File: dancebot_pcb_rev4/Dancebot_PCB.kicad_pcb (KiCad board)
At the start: 2 copper layers, 53.3 x 63.5 mm, 52 parts, among them J1 Voltage Regulator, J10 NeoPixel Right Eye, J11 Rocker Switch, J2 IO14 servo 1, J3 IO13 servo 2, J4 IO12 servo 3, J5 IO15 servo 4, J6 IO18 servo 5 (hat), J7 UJ2-MIBH2-4-SMT-TR, J8 Pins, J9 NeoPixel Left Eye, Q1 IRLML6402TRPBF, Q2 S8050, Q3 S8050, SW1 RESET, SW2 BOOT, U1 IRLML2502TRPBF, U2 AMS1117-3.3, U3 ESP32-WROOM-32E__4MB_, U4 CP2102N-A02-GQFN28R

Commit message: schematic ready for review!
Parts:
- removed C1: 4.7u, Capacitor_SMD:C_0805_2012Metric
- removed C2: 0.1u, Capacitor_SMD:C_0805_2012Metric
- removed C5: 10u, Capacitor_SMD:C_0805_2012Metric
- removed C6: 22u, Capacitor_SMD:C_0805_2012Metric
- removed D2: 1N5819, Diode_THT:D_DO-41_SOD81_P10.16mm_Horizontal
- removed H4: ~, MountingHole:MountingHole_3.2mm_M3
- removed J1: Voltage Regulator, Connector_PinHeader_2.54mm:PinHeader_1x05_P2.54mm_Vertical
- removed J10: NeoPixel Right Eye, Connector_PinSocket_2.54mm:PinSocket_1x04_P2.54mm_Vertical
- removed J11: Rocker Switch, Connector_PinHeader_2.54mm:PinHeader_1x02_P2.54mm_Vertical
- removed J5: IO15 servo 4, Connector_PinHeader_2.54mm:PinHeader_1x03_P2.54mm_Vertical
- removed J6: IO18 servo 5 (hat), Connector_PinHeader_2.54mm:PinHeader_1x03_P2.54mm_Vertical
- removed J8: Pins, Connector_PinHeader_2.54mm:PinHeader_1x02_P2.54mm_Vertical
- removed TP4: TestPoint, TestPoint:TestPoint_Pad_2.0x2.0mm
- removed U2: AMS1117-3.3, AMS1117-3.3:SOT229P700X180-4N
- removed U3: ESP32-WROOM-32E__4MB_, ESP32-WROOM-32E__4MB_:XCVR_ESP32-WROOM-32E__4MB_
- removed U4: CP2102N-A02-GQFN28R, CP2102N-A02-GQFN28R:IC_CP2102N-A02-GQFN28R
- added C10: 4.7u, SamacSys_Parts:CAPC2013X140N, F.Cu at (252.8, 106.9)
- added C11: 0.1u, SamacSys_Parts:MAJx16, F.Cu at (238.9, 108.5)
- added C201: 1u, SamacSys_Parts:CAPC2012X135N, F.Cu at (221.0, 103.3)
- added C202: 1u, SamacSys_Parts:CAPC2012X135N, F.Cu at (221.0, 106.0)
- added C203: 0.1u, SamacSys_Parts:MAJx16, F.Cu at (215.5, 109.6)
- added C204: 10u, SamacSys_Parts:CAPC1608X80N, F.Cu at (208.1, 109.5)
- added C205: 0.1u, SamacSys_Parts:MAJx16, F.Cu at (215.5, 113.5)
- added C206: 10u, SamacSys_Parts:CAPC1608X80N, F.Cu at (208.1, 111.8)
- added C207: 10u, SamacSys_Parts:CAPC1608X80N, F.Cu at (208.1, 114.1)
- added D201: SMF5.0A_R1_00001, SamacSys_Parts:SMF50A_R1_00001, F.Cu at (221.8, 116.2)
- added D202: LM66100DCKR, SamacSys_Parts:SOP65P210X110-6N, F.Cu at (204.0, 110.2)
- added D203: LM66100DCKR, SamacSys_Parts:SOP65P210X110-6N, F.Cu at (204.0, 113.9)
- added D3: SMF5.0A_R1_00001, SamacSys_Parts:SMF50A_R1_00001, F.Cu at (239.9, 99.2)
- added D303: SMF5.0A_R1_00001, SamacSys_Parts:SMF50A_R1_00001, F.Cu at (239.9, 104.1)
- added H5: MountingHole_Pad, MountingHole:MountingHole_3.2mm_M3, F.Cu at (240.2, 85.9)
- added IC1: CP2102N-A02-GQFN28R, SamacSys_Parts:QFN50P500X500X80-29N-D, F.Cu at (247.2, 103.0)
- added IC2: ESP32-WROOM-32E-N4, SamacSys_Parts:ESP32WROOM32EN4, F.Cu at (212.7, 72.4)
- added IC201: TPS63000IDRCRQ1, SamacSys_Parts:TPS63000IDRCRQ1, F.Cu at (222.3, 98.7)
- added J12: USB_B_Micro, Connector_USB:USB_Micro-B_Amphenol_10118193-0002LF_Horizontal, F.Cu at (248.7, 96.2)
- added J13: Servo 4, Connector_PinHeader_2.54mm:PinHeader_1x03_P2.54mm_Vertical, F.Cu at (252.3, 114.8)
- added J14: Servo 5, Connector_PinHeader_2.54mm:PinHeader_1x03_P2.54mm_Vertical, F.Cu at (256.9, 114.8)
- added J201: BatteryJ ST Connector, SamacSys_Parts:1769, F.Cu at (207.3, 99.6)
- added L201: 2.2u, SamacSys_Parts:NRS3015T2R2MNGHV, F.Cu at (221.2, 110.7)
- added LED1: APT2012PGW, SamacSys_Parts:APT2012PGW, F.Cu at (258.8, 60.2)
- added R201: 100, SamacSys_Parts:RESC2012X50N, F.Cu at (208.6, 116.8)
- added R202: 1M, SamacSys_Parts:RESC2012X60N, F.Cu at (215.2, 116.9)
- added R203: 200k, SamacSys_Parts:RESC1608X55N, F.Cu at (203.7, 117.0)
- added TP201: USBV, TestPoint:TestPoint_Pad_1.0x1.0mm, F.Cu at (214.4, 103.0)
- added TP202: BATV, TestPoint:TestPoint_Pad_1.0x1.0mm, F.Cu at (214.4, 106.1)
- added TP203: BUCK_VIN, TestPoint:TestPoint_Pad_1.0x1.0mm, F.Cu at (217.5, 96.9)
- added TP204: GND, TestPoint:TestPoint_Pad_1.0x1.0mm, F.Cu at (217.5, 100.0)
- added TP205: 3v3, TestPoint:TestPoint_Pad_1.0x1.0mm, F.Cu at (217.5, 103.0)
- C3, C4, C8: footprint Capacitor_SMD:C_0805_2012Metric -> SamacSys_Parts:MAJx16
- C7: footprint Capacitor_SMD:C_0805_2012Metric -> SamacSys_Parts:CAPC2012X145N
- C9: footprint Capacitor_SMD:C_0805_2012Metric -> SamacSys_Parts:CAPC2012X135N
- D1: value LED -> SMF5.0A_R1_00001; footprint LED_SMD:LED_0805_2012Metric -> SamacSys_Parts:SMF50A_R1_00001
- H1, H2, H3: value ~ -> MountingHole_Pad
- J2: value IO14 servo 1 -> Servo 1
- J3: value IO13 servo 2 -> Servo 2
- J4: value IO12 servo 3 -> NeoPixel Left Eye; footprint Connector_PinHeader_2.54mm:PinHeader_1x03_P2.54mm_Vertical -> Connector_PinSocket_2.54mm:PinSocket_1x04_P2.54mm_Vertical
- J7: value UJ2-MIBH2-4-SMT-TR -> Servo #; footprint UJ2-MIBH-4-SMT-TR:CUIDEVICES_UJ2-MIBH-4-SMT-TR -> Connector_PinHeader_2.54mm:PinHeader_1x03_P2.54mm_Vertical
- Q1: footprint IRLML6402TRPBF:SOT95P237X112-3N -> SamacSys_Parts:SOT95P237X112-3N
- Q2, Q3: footprint Package_TO_SOT_THT:TO-92_Inline -> SamacSys_Parts:SOT95P240X115-3N
- R1, R2, R4, R5, R6, R7: footprint Resistor_SMD:R_0805_2012Metric -> SamacSys_Parts:RESC2012X50N
- R10, R13, R8, R9: footprint Resistor_SMD:R_0805_2012Metric -> SamacSys_Parts:RESC2012X60N
- R11, R12: value 2k -> 1k; footprint Resistor_SMD:R_0805_2012Metric -> SamacSys_Parts:RESC2012X60N
- R3: footprint Resistor_SMD:R_0805_2012Metric -> SamacSys_Parts:ERA6AEB101V
- SW1, SW2: footprint Button_Switch_THT:KSA_Tactile_SPST -> SamacSys_Parts:SW_PUSH_6mm
- TP1: value TestPoint -> BATT_ADC; footprint TestPoint:TestPoint_Pad_2.0x2.0mm -> TestPoint:TestPoint_Pad_1.0x1.0mm
- TP2: value TestPoint -> USBC_ST; footprint TestPoint:TestPoint_Pad_2.0x2.0mm -> TestPoint:TestPoint_Pad_1.0x1.0mm
- TP3: value TestPoint -> BAT_ST; footprint TestPoint:TestPoint_Pad_2.0x2.0mm -> TestPoint:TestPoint_Pad_1.0x1.0mm
- U1: footprint IRLML2502TRPBF:SOT23 -> SamacSys_Parts:SOT95P237X112-3N
- moved TP1 101.8 mm to (257.2, 73.8), turned to 0 degrees
- moved H2 100.4 mm to (240.2, 70.0), turned to 0 degrees
- moved R8 91.6 mm to (253.1, 100.9), turned to 0 degrees
- moved J4 91.5 mm to (248.6, 60.4), turned to 0 degrees
- moved H1 89.8 mm to (240.2, 62.0), turned to 0 degrees
- moved J3 88.8 mm to (243.2, 114.8), turned to 0 degrees
- moved R3 88.3 mm to (254.4, 83.7), turned to 0 degrees
- moved R11 86.4 mm to (257.6, 63.9), turned to 0 degrees
- moved Q1 84.7 mm to (253.2, 74.6), turned to 0 degrees
- moved R7 84.0 mm to (245.9, 108.2), turned to 0 degrees
- moved R2 83.0 mm to (248.5, 76.9), turned to 0 degrees
- moved J2 80.7 mm to (238.6, 114.8), turned to 0 degrees
- moved C3 77.0 mm to (226.3, 77.1), turned to 0 degrees
- moved R1 76.7 mm to (248.5, 73.8)
- moved R4 75.6 mm to (248.5, 79.9), turned to 0 degrees
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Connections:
- net BATT ADC renamed /BATTERY_STAT/BATT_ADC
- net DTR renamed /MCU/UART.DTR
- net EN renamed /MCU/EN
- net IO0 renamed /MCU/IO0
- net RTS renamed /MCU/UART.RTS
- C7 pad 1: 3v3 -> +3V3
- C8 pad 1: 3v3 -> +3V3
- D1 pad 1: Net-(D1-K) -> /MCU/D+
- D1 pad 2: 3v3 -> GND
- J2 pad 1: SM1 -> /MCU/SM1
- J2 pad 2: VBUS -> +3V3
- J3 pad 1: SM2 -> /MCU/SM2
- J3 pad 2: VBUS -> +3V3
- J4 pad 1: SM3 -> GND
- J4 pad 2: VBUS -> /LEDS/NP2_DIN
- J4 pad 3: GND -> /LEDS/NP2_DOUT
- J7 pad 1: VBUS -> /MCU/SM3
- J7 pad 2: D- -> +3V3
- J7 pad 3: D+ -> GND
- J9 pad 1: unconnected-(J9-Pin_1-Pad1) -> GND
- J9 pad 2: GND -> /LEDS/NP1_DIN
- J9 pad 3: VOUT -> /LEDS/NP1_DOUT
- J9 pad 4: NPLeftEye -> +3V3
- R11 pad 1: 3v3 -> Net-(LED1-K)
- R11 pad 2: Net-(U4-~{RST}) -> GND
- R12 pad 1: Net-(D1-K) -> +3V3
- R12 pad 2: GND -> Net-(IC1-RSTB)
- R13 pad 1: 3v3 -> +3V3
- R4 pad 1: BATT EN -> /BATTERY_STAT/BATT_EN
- R7 pad 1: VBUS -> /POWER/USB_VBUS
- TP2 pad 1: NPLeftEye -> /POWER/USBC_ST
- TP3 pad 1: NPRightEye -> /POWER/BAT_ST
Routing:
- net SM5: track 15.5 -> 0.00 mm
- net SM4: track 13.5 -> 0.00 mm
- net SM3: track 11.9 -> 0.00 mm
- net D+: track 11.8 -> 0.00 mm, vias 1 -> 0
- net SM2: track 8.71 -> 0.00 mm
- net D-: track 8.27 -> 0.00 mm
- net SM1: track 7.31 -> 0.00 mm
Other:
- board size 53.3 x 63.5 mm -> 53.9 x 63.5 mm
- board text removed: "ADC"
- board text removed: "BATTPWR"
- board text removed: "L"
- board text removed: "R"
- board text removed: "aL"
- board text removed: "aR"
- board text removed: "hL"
- board text removed: "hR"
- board text removed: "hat"

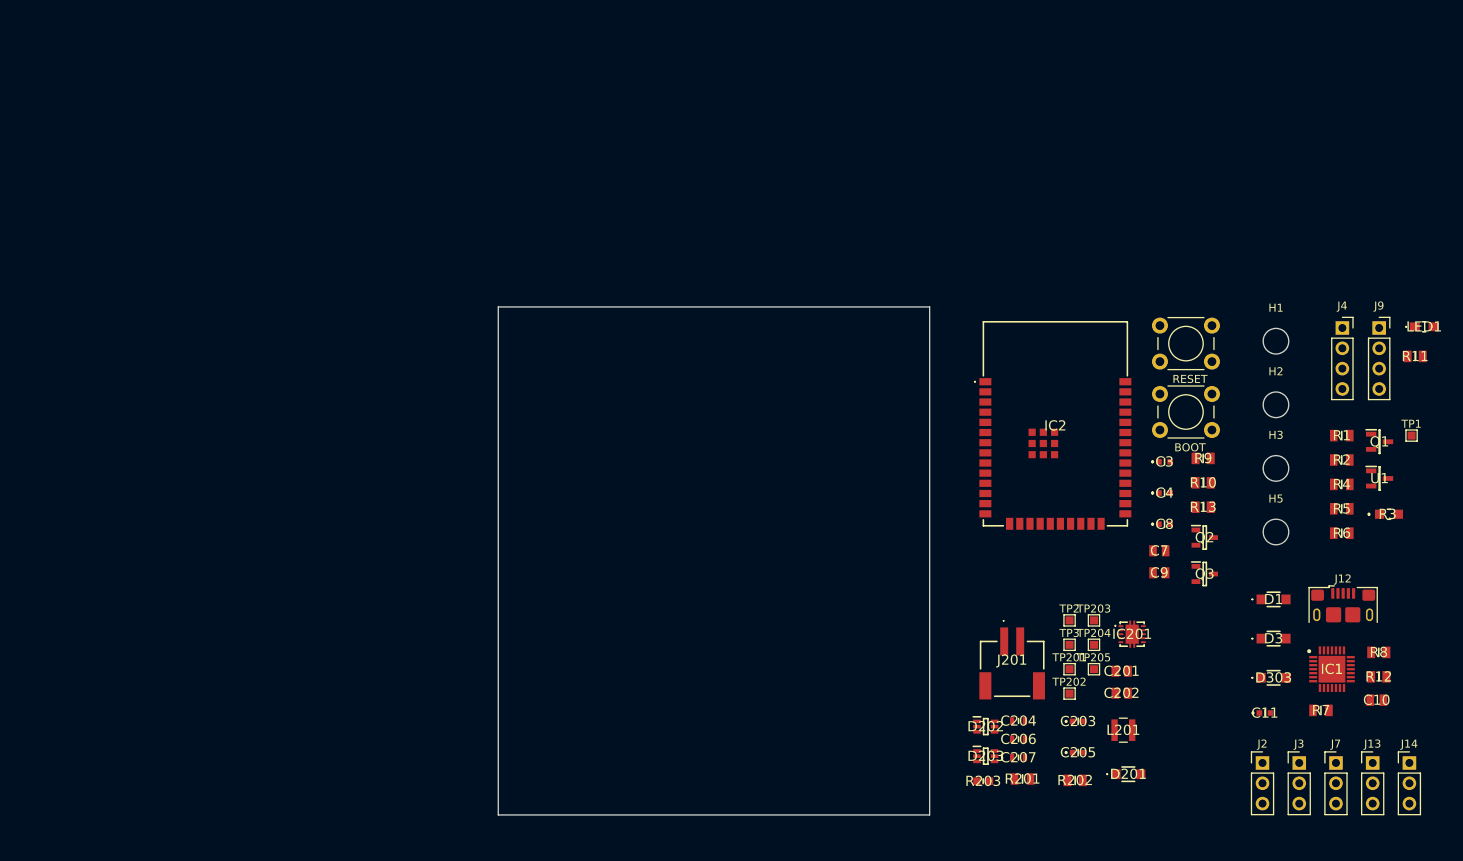
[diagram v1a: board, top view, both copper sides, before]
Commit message: now using ESP32-S3-WROOM-1, changed power delivery system
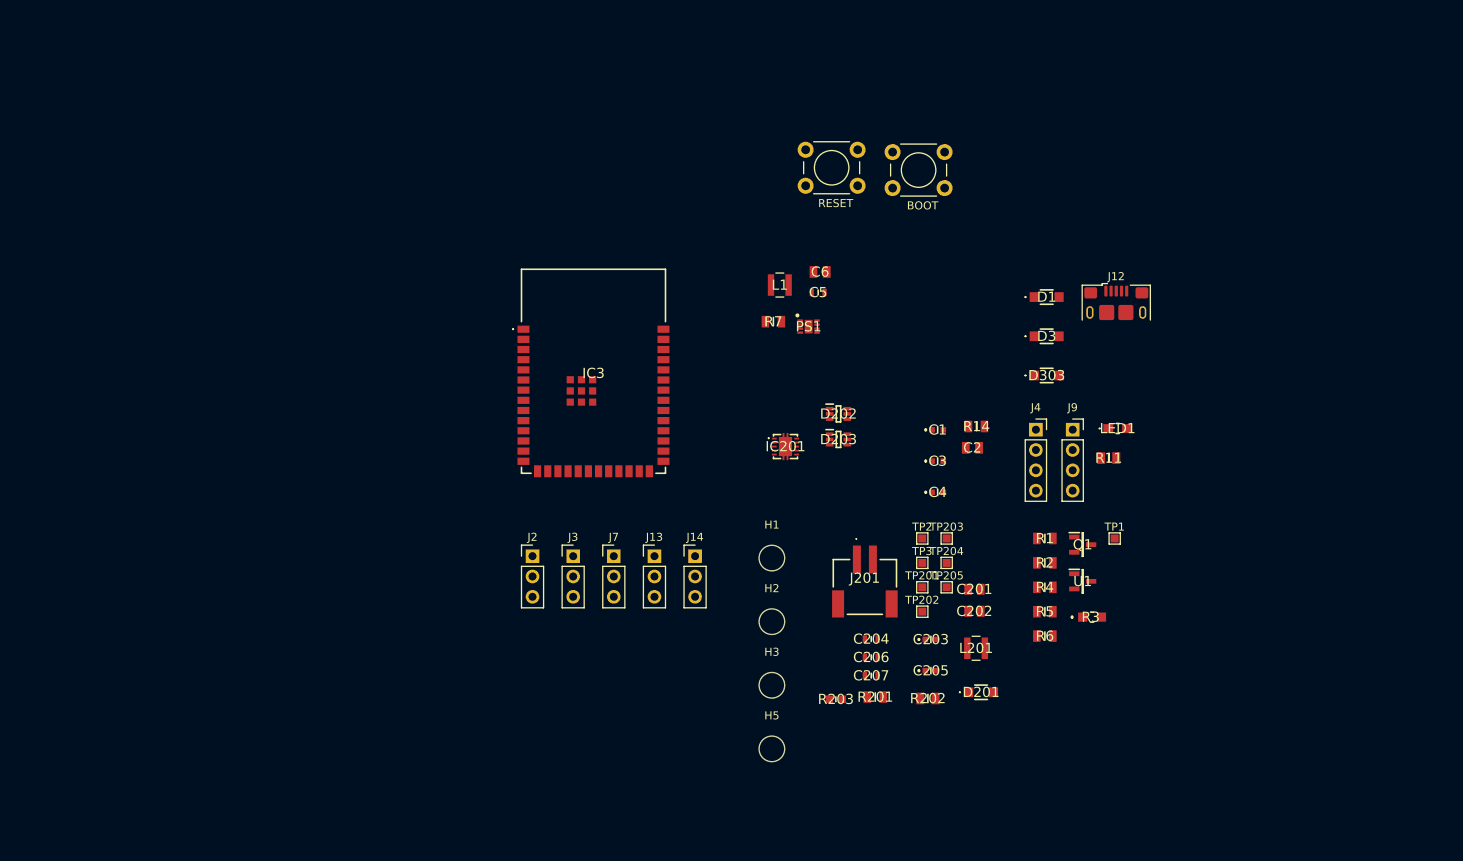
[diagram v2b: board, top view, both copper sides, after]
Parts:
- removed C10: 4.7u, SamacSys_Parts:CAPC2013X140N
- removed C11, C8: 0.1u, SamacSys_Parts:MAJx16
- removed C7: 22u, SamacSys_Parts:CAPC2012X145N
- removed C9: 1u, SamacSys_Parts:CAPC2012X135N
- removed IC1: CP2102N-A02-GQFN28R, SamacSys_Parts:QFN50P500X500X80-29N-D
- removed IC2: ESP32-WROOM-32E-N4, SamacSys_Parts:ESP32WROOM32EN4
- removed Q2, Q3: S8050, SamacSys_Parts:SOT95P240X115-3N
- removed R10, R13, R9: 10k, SamacSys_Parts:RESC2012X60N
- removed R12: 1k, SamacSys_Parts:RESC2012X60N
- removed R8: 47.5k, SamacSys_Parts:RESC2012X60N
- added C1: 0.1u, SamacSys_Parts:MAJx16, F.Cu at (198.0, 73.1)
- added C2: 22u, SamacSys_Parts:CAPC2012X145N, F.Cu at (202.3, 75.4)
- added C5: 10u, SamacSys_Parts:CAPC1608X80N, F.Cu at (183.0, 55.9)
- added C6: 22u, SamacSys_Parts:CAPC2012X145N, F.Cu at (183.3, 53.4)
- added IC3: ESP32-S3-WROOM-1-N4, SamacSys_Parts:ESP32S3WROOM1N4, F.Cu at (154.9, 66.0)
- added L1: 2.2u, SamacSys_Parts:NRS3015T2R2MNGHV, F.Cu at (178.2, 55.0)
- added PS1: TPS62163DSGR, SamacSys_Parts:SON50P200X200X80-9N, F.Cu at (181.8, 60.2)
- added R14: 10k, SamacSys_Parts:RESC2012X50N, F.Cu at (202.8, 72.7)
- R7: value 22.1k -> 100k
- moved J2 94.8 mm to (147.3, 88.9)
- moved J3 94.4 mm to (152.4, 88.9)
- moved J7 93.9 mm to (157.5, 88.9)
- moved J13 93.4 mm to (162.6, 88.9)
- moved J14 93.0 mm to (167.6, 88.9)
- moved R7 83.9 mm to (177.4, 59.6)
- moved H1 68.6 mm to (177.2, 89.1)
- moved H2 68.6 mm to (177.2, 97.1)
- moved H3 68.6 mm to (177.2, 105.0)
- moved H5 68.6 mm to (177.2, 113.0)
- moved SW1 49.4 mm to (181.5, 38.1)
- moved IC201 49.3 mm to (178.9, 75.2)
- moved J12 47.2 mm to (220.3, 58.4)
- moved D1 47.2 mm to (211.6, 56.5)
- moved D3 47.2 mm to (211.6, 61.4)
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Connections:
- net BATT PWR renamed /BATTERY_STAT/BAT_VBUS
- C202 pad 1: /POWER/BAT_VBUS -> Net-(D202-~{CE})
- C203 pad 1: /POWER/BUCK_VIN -> +5V
- C204 pad 1: /POWER/BUCK_VIN -> +5V
- D202 pad 3: /POWER/BAT_VBUS -> Net-(D202-~{CE})
- D202 pad 6: /POWER/BUCK_VIN -> +5V
- D203 pad 1: /POWER/BAT_VBUS -> Net-(D202-~{CE})
- D203 pad 6: /POWER/BUCK_VIN -> +5V
- IC201 pad 5: /POWER/BUCK_VIN -> +5V
- J13 pad 2: +3V3 -> +5V
- J14 pad 2: +3V3 -> +5V
- J2 pad 2: +3V3 -> +5V
- J3 pad 2: +3V3 -> +5V
- J7 pad 2: +3V3 -> +5V
- R201 pad 1: /POWER/BUCK_VIN -> +5V
- R7 pad 1: /POWER/USB_VBUS -> Net-(PS1-PG)
- R7 pad 2: Net-(IC1-VBUS) -> Net-(D202-~{CE})
- TP203 pad 1: /POWER/BUCK_VIN -> +5V
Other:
- board outline removed

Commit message: first routing iteration
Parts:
- removed TP203: BUCK_VIN, TestPoint:TestPoint_Pad_1.0x1.0mm
- added TP4: 5v, TestPoint:TestPoint_Pad_1.0x1.0mm, F.Cu at (99.8, 102.6)
- moved J12 136.2 mm to (85.3, 76.7), turned to -90 degrees
- moved LED1 134.3 mm to (86.5, 63.0)
- moved R11 133.4 mm to (86.3, 66.3)
- moved J9 121.4 mm to (93.7, 64.5), turned to 90 degrees
- moved D3 117.0 mm to (95.2, 73.7)
- moved J4 116.6 mm to (93.7, 69.3), turned to 90 degrees
- moved D1 111.1 mm to (102.9, 79.5)
- moved SW2 109.8 mm to (93.5, 86.1)
- moved D303 108.9 mm to (102.9, 73.4)
- moved TP3 101.6 mm to (95.2, 102.4)
- moved TP2 101.5 mm to (95.2, 98.6)
- moved R14 101.4 mm to (103.1, 54.4), turned to -90 degrees
- moved C3 96.5 mm to (103.1, 59.4), turned to -90 degrees
- moved H1 96.1 mm to (86.9, 56.4)
- moved C2 95.6 mm to (108.2, 58.7), turned to 90 degrees
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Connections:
- C5 pad 1: /POWER/BAT_VBUS -> /BATTERY_STAT/BAT_VBUS
- D201 pad 1: /POWER/BAT_VBUS -> /BATTERY_STAT/BAT_VBUS
- J201 pad 1: /POWER/BAT_VBUS -> /BATTERY_STAT/BAT_VBUS
- PS1 pad 2: /POWER/BAT_VBUS -> /BATTERY_STAT/BAT_VBUS
- PS1 pad 3: /POWER/BAT_VBUS -> /BATTERY_STAT/BAT_VBUS
- TP202 pad 1: /POWER/BAT_VBUS -> /BATTERY_STAT/BAT_VBUS
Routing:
- net +3V3: track 0.00 -> 102.3 mm, vias 0 -> 3
- net +5V: track 0.00 -> 71.2 mm, vias 0 -> 1
- net /POWER/USB_VBUS: track 0.00 -> 67.5 mm, vias 0 -> 2
- net /BATTERY_STAT/BAT_VBUS: track 0.00 -> 65.1 mm, vias 0 -> 2
- net /MCU/IO0: track 0.00 -> 49.3 mm, vias 0 -> 2
- net GND: track 0.00 -> 36.3 mm, vias 0 -> 1
- net /BATTERY_STAT/BATT_EN: track 0.00 -> 32.1 mm, vias 0 -> 2
- net /MCU/D+: track 0.00 -> 27.5 mm
- net /MCU/D-: track 0.00 -> 27.4 mm
- net Net-(D202-~{CE}): track 0.00 -> 25.1 mm
- net /MCU/EN: track 0.00 -> 22.2 mm
- net /BATTERY_STAT/BATT_ADC: track 0.00 -> 20.6 mm
- net /LEDS/NP1_DIN: track 0.00 -> 17.6 mm
- net /LEDS/NP2_DIN: track 0.00 -> 16.3 mm
- net /LEDS/NP1_DOUT: track 0.00 -> 14.3 mm
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- added copper zone on B.Cu, net GND
- added copper zone on F.Cu, net GND
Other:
- board outline added: 66 x 53.3 mm
- board text added: "+3v3"
- board text added: "+5v"
- board text added: "BAT_ADC"
- board text added: "BAT_ST"
- board text added: "BAT_VBUS"
- board text added: "GND"
- board text added: "POWER ON"
- board text added: "USB_ST"
- board text added: "USB_VBUS"

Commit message: implemented some changes
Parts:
- added LED2: APT2012PGW, SamacSys_Parts:APT2012PGW, F.Cu at (145.1, 70.6)
- added R8: 1k, SamacSys_Parts:RESC2012X60N, F.Cu at (145.4, 73.7)
- moved C1 3.81 mm to (108.0, 58.7)
- moved L201 3.05 mm to (133.9, 84.3), turned to 90 degrees
- moved C2 3.05 mm to (105.2, 58.7)
- moved IC201 1.91 mm to (139.3, 86.9)
- moved SW1 1.22 mm to (92.3, 54.1)
- moved H2 1.08 mm to (86.1, 102.4)
- moved H3 1.08 mm to (145.5, 55.6)
- moved H5 1.08 mm to (145.5, 102.4)
- moved R14 1.02 mm to (102.1, 54.3)
- moved C3 1.02 mm to (102.1, 59.4)
- moved H1 0.92 mm to (86.1, 55.9)
- moved D3 0.25 mm to (95.2, 73.4)
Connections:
- IC3 pad 26: unconnected-(IC3-IO45-Pad26) -> /LEDS/IO45
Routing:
- net /LEDS/IO45: track 0.00 -> 20.2 mm
- net +5V: track 71.2 -> 75.7 mm
- net +3V3: track 102.3 -> 106.8 mm
- net Net-(LED2-K): track 0.00 -> 3.05 mm
- net Net-(IC201-L1): track 7.72 -> 4.87 mm
- net /MCU/EN: track 22.2 -> 24.8 mm
- net /BATTERY_STAT/BATT_ADC: track 20.6 -> 19.1 mm
- net /BATTERY_STAT/BAT_VBUS: track 65.1 -> 66.2 mm
- net /POWER/USB_VBUS: track 67.5 -> 68.3 mm
- net GND: track 36.3 -> 35.8 mm, vias 1 -> 5
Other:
- outline, holes or cut-outs redrawn
- board text added: "Dancebot v4 Arsen Iman Toby Nguyen"
- board text added: "GND 5v PWM"
- board text added: "GND IN OUT 3v3"
- board text added: "GPIO"
- board text added: "Left Right"
- board text added: "Servo 1"
- board text added: "Servo 5"
